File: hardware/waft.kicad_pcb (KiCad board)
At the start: 2 copper layers, 45 parts, among them IC1 VL6180x_Composite, J1 CONN_01X01, J2 Thonkiconn, J3 Thonkiconn, J4 Thonkiconn, J5 Thonkiconn, J6 Thonkiconn, J7 Thonkiconn, U1 MCP4728, U2 TL071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

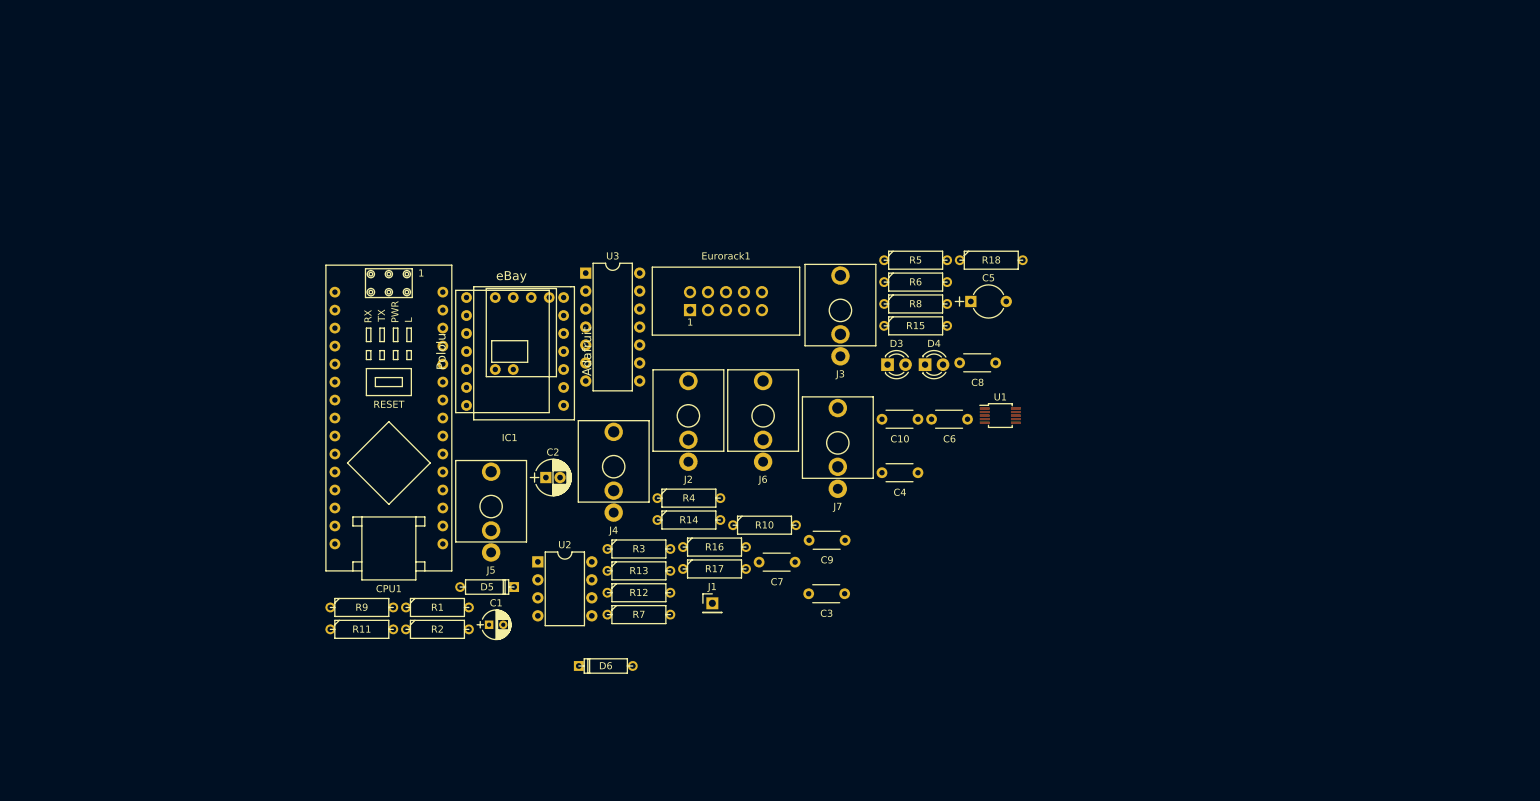
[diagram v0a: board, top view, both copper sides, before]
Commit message: Schematic changes.
Couple of changes to the schematic, & started laying out the PCB.
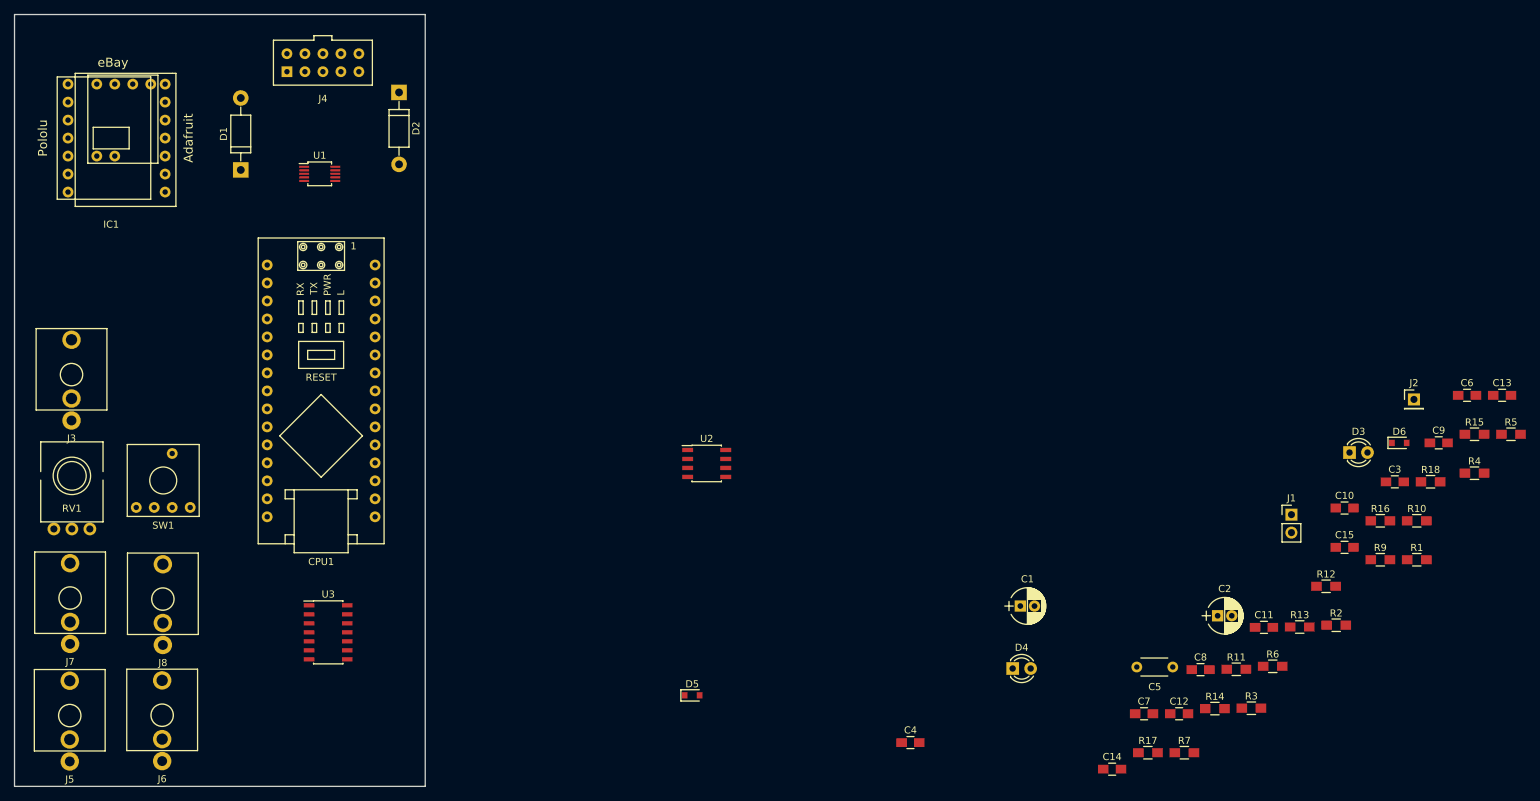
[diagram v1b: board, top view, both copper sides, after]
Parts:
- removed Eurorack1: CONN_02X05, Connect:IDC_Header_Straight_10pins
- removed R8: 100k, Discret:R3-5
- added C11: 47pF, Capacitors_SMD:C_0805_HandSoldering, F.Cu at (217.3, 137.9)
- added C12: 47pF, Capacitors_SMD:C_0805_HandSoldering, F.Cu at (205.3, 150.1)
- added C13: 47pF, Capacitors_SMD:C_0805_HandSoldering, F.Cu at (250.9, 105.2)
- added C14: 47pF, Capacitors_SMD:C_0805_HandSoldering, F.Cu at (195.9, 158.0)
- added C15: 47pF, Capacitors_SMD:C_0805_HandSoldering, F.Cu at (228.7, 126.6)
- added D1: 1N5817, Diodes_ThroughHole:D_DO-41_SOD81_P10.16mm_Horizontal, F.Cu at (72.8, 73.3)
- added D2: 1N5817, Diodes_ThroughHole:D_DO-41_SOD81_P10.16mm_Horizontal, F.Cu at (95.2, 62.4)
- added J8: Thonkiconn, europi:Thonkiconn, F.Cu at (61.8, 133.9)
- added RV1: B100K, europi:Alpha_9mm_Vertical, F.Cu at (49.0, 116.5)
- added SW1: Coded_Switch, europi:10_Way_Coded_Switch, F.Cu at (61.9, 117.2)
- C1: footprint Capacitors_ThroughHole:CP_Radial_D4.0mm_P2.00mm -> Capacitors_ThroughHole:CP_Radial_D5.0mm_P2.00mm
- C10, C3, C4, C6, C7, C8, C9: footprint europi:tantalum_capacitor -> Capacitors_SMD:C_0805_HandSoldering
- C5: footprint Capacitors_ThroughHole:CP_Radial_Tantal_D4.5mm_P5.00mm -> europi:tantalum_capacitor
- D5, D6: footprint Discret:D3 -> Diodes_SMD:D_0805
- J1: value CONN_01X01 -> CONN_01X02; footprint Pin_Headers:Pin_Header_Straight_1x01_Pitch2.54mm -> Pin_Headers:Pin_Header_Straight_1x02_Pitch2.54mm
- J2: value Thonkiconn -> CONN_01X01; footprint europi:Thonkiconn -> Pin_Headers:Pin_Header_Straight_1x01_Pitch2.54mm
- J4: value Thonkiconn -> Conn_02x05_Odd_Even; footprint europi:Thonkiconn -> europi:IDC-2x5
- R1, R10, R11, R12, R13, R14, R15, R16, R17, R18, R2, R3, R4, R5, R6, R7, R9: footprint Discret:R3-5 -> Resistors_SMD:R_0805_HandSoldering
- U2: footprint Housings_DIP:DIP-8_W7.62mm -> Housings_SOIC:SOIC-8_3.9x4.9mm_Pitch1.27mm
- U3: footprint Housings_DIP:DIP-14_W7.62mm -> Housings_SOIC:SOIC-14_3.9x8.7mm_Pitch1.27mm
- moved R9 144.0 mm to (233.7, 128.4)
- moved R1 138.5 mm to (238.9, 128.4)
- moved R2 126.9 mm to (227.5, 137.6)
- moved R11 123.6 mm to (213.4, 143.9)
- moved D6 116.4 mm to (236.4, 111.9), turned to 0 degrees
- moved R4 111.0 mm to (247.0, 116.2)
- moved J7 110.6 mm to (48.7, 133.8)
- moved J3 109.0 mm to (48.9, 102.2)
- moved J2 102.5 mm to (238.5, 105.8)
- moved U1 102.0 mm to (84.0, 73.9)
- moved R12 97.0 mm to (226.1, 132.1)
- moved C2 96.8 mm to (210.8, 136.3)
- moved J6 94.8 mm to (61.7, 150.3)
- moved R16 94.1 mm to (233.7, 122.9)
- moved R13 93.7 mm to (222.3, 137.9)
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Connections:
- CPU1 pad 10: (no net) -> Net-(CPU1-Pad10)
- CPU1 pad 11: (no net) -> Net-(CPU1-Pad11)
- CPU1 pad 12: (no net) -> Net-(CPU1-Pad12)
- CPU1 pad 13: (no net) -> Net-(CPU1-Pad13)
- CPU1 pad 9: (no net) -> DIR
- J1 pad 1: Net-(J1-Pad1) -> GND
- J2 pad 1: GND -> Net-(J2-Pad1)
- J3 pad 2: (no net) -> GND
- J4 pad 1: GND -> Net-(D1-Pad2)
- J4 pad 2: (no net) -> Net-(D1-Pad2)
- J4 pad 3: Net-(D5-Pad1) -> GND
- J5 pad 3: Net-(D6-Pad1) -> Net-(D5-Pad1)
- J6 pad 3: Net-(J6-Pad3) -> Net-(D6-Pad1)
- R1 pad 1: Net-(J1-Pad1) -> Net-(J2-Pad1)
- R17 pad 1: Net-(J6-Pad3) -> Net-(J7-Pad3)
- R18 pad 1: Net-(J7-Pad3) -> Net-(J8-Pad3)
- R2 pad 2: Net-(J1-Pad1) -> Net-(J2-Pad1)
- R4 pad 1: Net-(R4-Pad1) -> Net-(C15-Pad1)
- R5 pad 2: Net-(J2-Pad3) -> Net-(J3-Pad3)
- R6 pad 2: Net-(R4-Pad1) -> Net-(R6-Pad2)
- U2 pad 6: Net-(R4-Pad1) -> Net-(C15-Pad1)
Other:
- board outline added: 58 x 109 mm
- rule pad_to_mask_clearance: 0.2 -> 0

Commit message: Started board layout
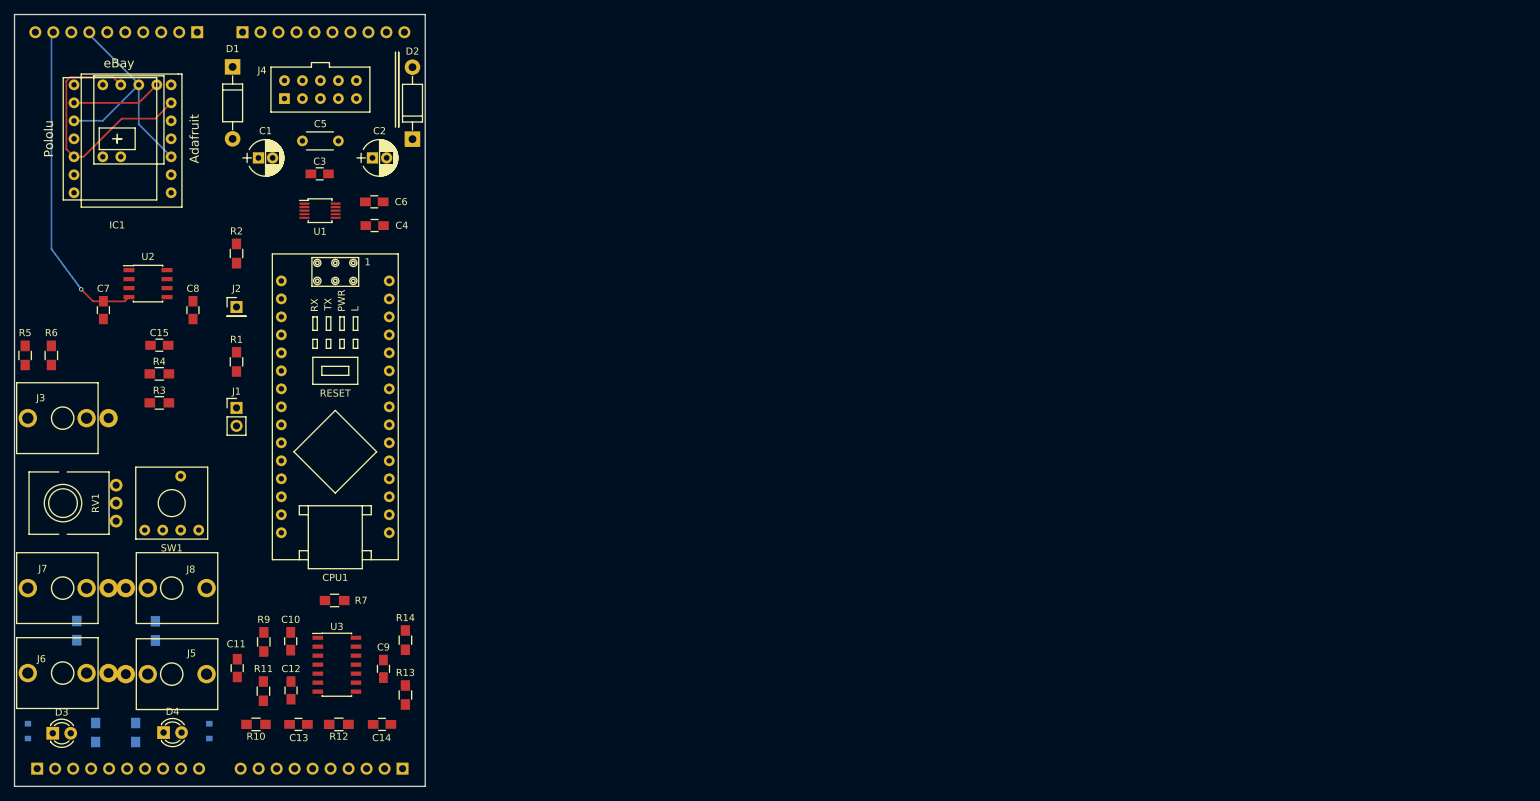
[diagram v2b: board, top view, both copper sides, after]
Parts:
- added J10: Conn_01x10_Female, Pin_Headers:Pin_Header_Straight_1x10_Pitch2.54mm, B.Cu at (95.7, 157.9)
- added J11: Conn_01x10_Male, Pin_Headers:Pin_Header_Straight_1x10_Pitch2.54mm, B.Cu at (66.7, 53.9)
- added J12: Conn_01x10_Male, Pin_Headers:Pin_Header_Straight_1x10_Pitch2.54mm, B.Cu at (44.0, 157.9)
- added J9: Conn_01x10_Female, Pin_Headers:Pin_Header_Straight_1x10_Pitch2.54mm, B.Cu at (73.0, 53.9)
- D5, D6, R15, R16, R17, R18: moved to B.Cu
- moved R5 210.1 mm to (42.4, 99.5), turned to 270 degrees
- moved R15 199.2 mm to (52.3, 152.8), turned to 270 degrees
- moved D3 187.4 mm to (46.2, 152.9)
- moved R4 186.3 mm to (61.3, 102.2), turned to 180 degrees
- moved R18 181.3 mm to (60.8, 138.4), turned to 270 degrees
- moved R16 178.3 mm to (58.0, 152.8), turned to 270 degrees
- moved R6 178.0 mm to (46.0, 99.5), turned to 270 degrees
- moved C13 176.2 mm to (81.0, 151.7), turned to 180 degrees
- moved D6 172.9 mm to (68.3, 152.6), turned to 270 degrees
- moved C15 169.8 mm to (61.3, 98.1), turned to 180 degrees
- moved R1 169.0 mm to (72.2, 100.5), turned to 270 degrees
- moved J2 166.8 mm to (72.2, 92.7)
- moved R10 166.4 mm to (75.0, 151.7), turned to 180 degrees
- moved R2 163.9 mm to (72.2, 85.2), turned to 270 degrees
- moved R3 160.1 mm to (61.3, 106.2)
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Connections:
- C11 pad 2: Net-(C11-Pad2) -> MIXa
- C13 pad 1: Net-(C13-Pad1) -> CV1a
- C14 pad 1: Net-(C14-Pad1) -> CV2a
- C6 pad 1: DAC_B -> DAC_Ba
- CPU1 pad 10: Net-(CPU1-Pad10) -> DOa
- CPU1 pad 11: Net-(CPU1-Pad11) -> D1a
- CPU1 pad 12: Net-(CPU1-Pad12) -> D2a
- CPU1 pad 13: Net-(CPU1-Pad13) -> D3a
- CPU1 pad 23: SDA -> SDAa
- CPU1 pad 24: SCL -> SCLa
- CPU1 pad 5: GATE_1 -> GATE_1a
- CPU1 pad 6: GATE_2 -> GATE_2a
- D5 pad 2: GATE_1 -> GATE_1b
- D6 pad 2: GATE_2 -> GATE_2b
- IC1 pad 19: SCL -> SCLb
- IC1 pad 20: SDA -> SDAb
- IC1 pad 4: SDA -> SDAb
- IC1 pad 5: SCL -> SCLb
- IC1 pad 8: SDA -> SDAb
- IC1 pad 9: SCL -> SCLb
- R13 pad 1: Net-(C13-Pad1) -> CV1a
- R14 pad 1: Net-(C14-Pad1) -> CV2a
- R15 pad 2: GATE_1 -> GATE_1b
- R16 pad 2: GATE_2 -> GATE_2b
- R17 pad 2: Net-(C13-Pad1) -> CV1b
- R18 pad 2: Net-(C14-Pad1) -> CV2b
- R5 pad 1: Net-(C11-Pad2) -> MIXb
- R6 pad 1: Net-(C11-Pad2) -> MIXb
- R9 pad 2: Net-(C11-Pad2) -> MIXa
- SW1 pad 2: Net-(CPU1-Pad10) -> D0b
- SW1 pad 3: Net-(CPU1-Pad11) -> D1b
- SW1 pad 4: Net-(CPU1-Pad12) -> D2b
- SW1 pad 5: Net-(CPU1-Pad13) -> D3b
- U1 pad 2: SCL -> SCLa
- U1 pad 3: SDA -> SDAa
- U1 pad 7: DAC_B -> DAC_Ba
- U2 pad 3: DAC_B -> DAC_Bb
- U3 pad 14: Net-(C14-Pad1) -> CV2a
- U3 pad 2: Net-(C11-Pad2) -> MIXa
- U3 pad 8: Net-(C13-Pad1) -> CV1a
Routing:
- net SCLb: track 0.00 -> 74.0 mm
- net GND: track 0.00 -> 23.4 mm
- net +3V3: track 0.00 -> 12.7 mm
- net MIXb: track 0.00 -> 10.3 mm
- net -12V: track 0.00 -> 7.67 mm, vias 0 -> 1

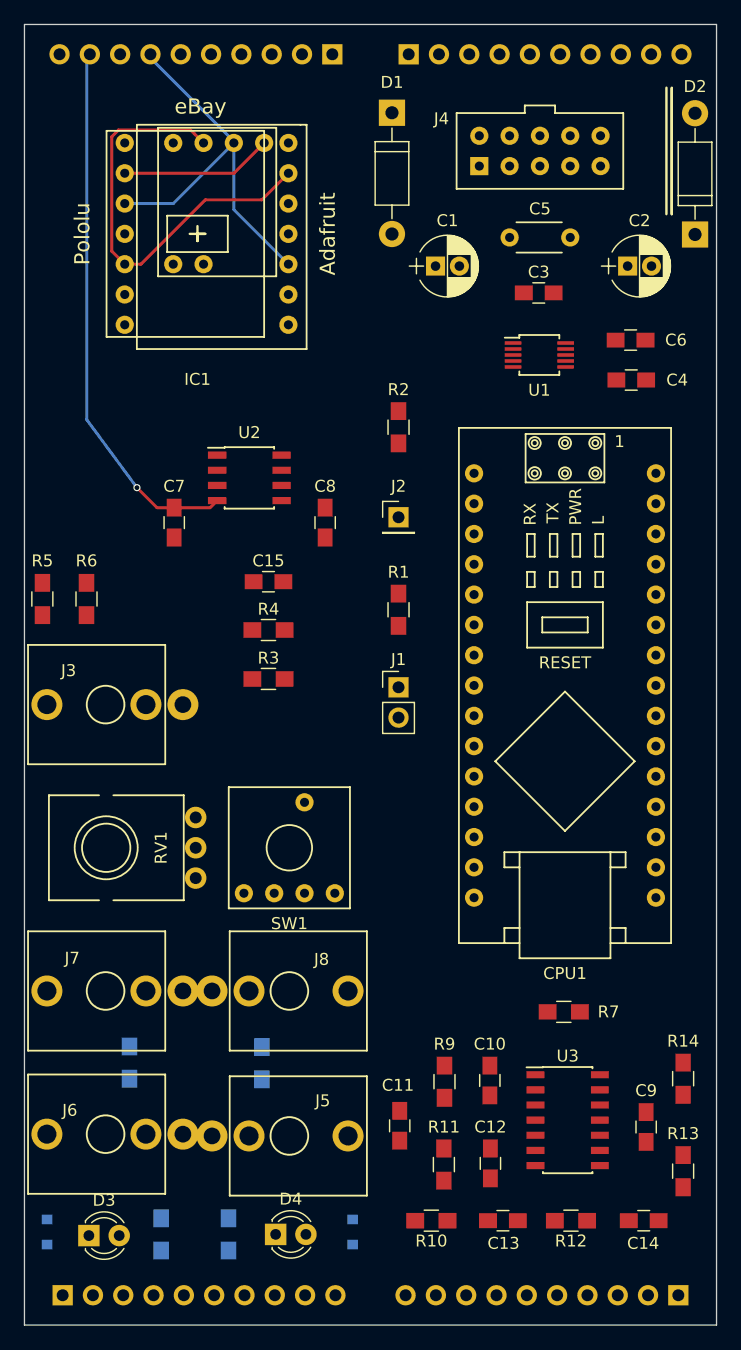
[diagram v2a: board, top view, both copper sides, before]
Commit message: Top and bottom track routing
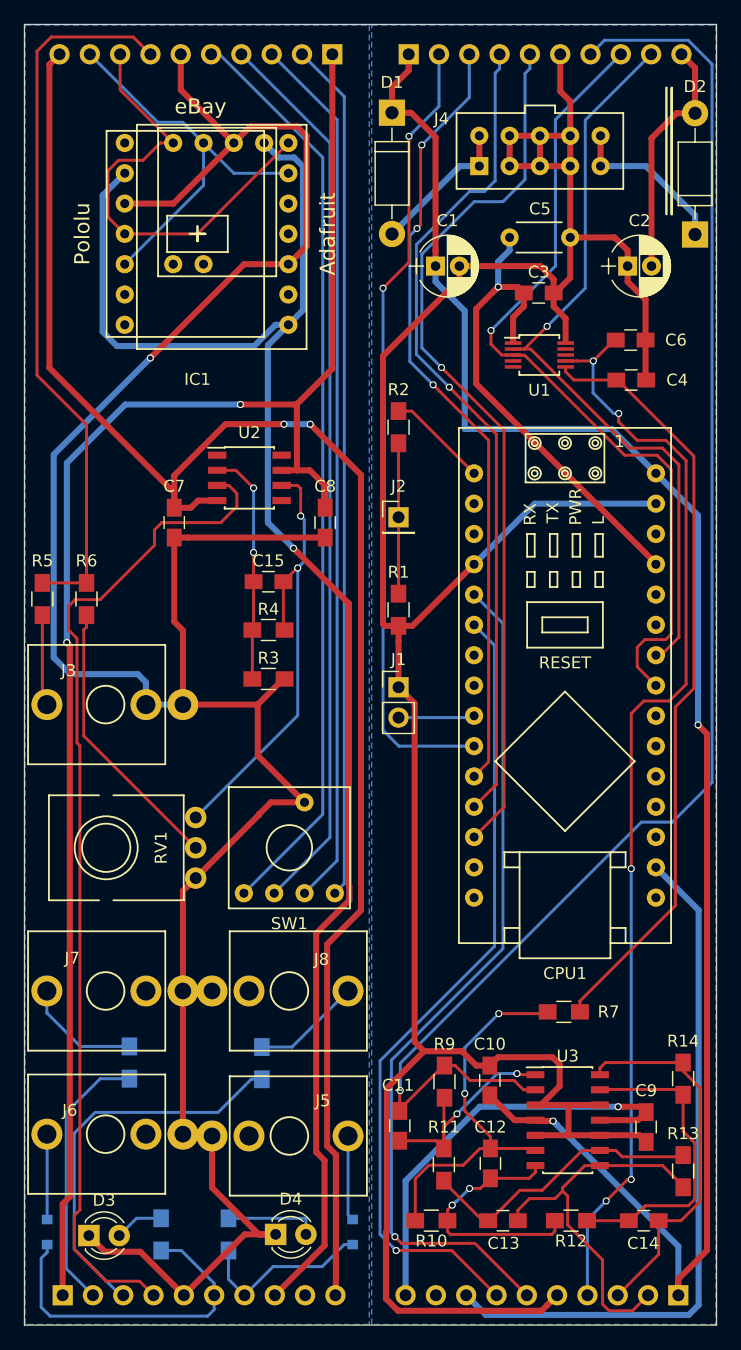
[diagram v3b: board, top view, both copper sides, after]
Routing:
- net GND: track 23.4 -> 446.9 mm, vias 0 -> 1
- net +12V: track 0.00 -> 283.4 mm, vias 0 -> 4
- net -12V: track 7.67 -> 195.2 mm, vias 1 -> 3
- net +3V3: track 12.7 -> 195.4 mm, vias 0 -> 1
- net MIXa: track 0.00 -> 125.5 mm, vias 0 -> 1
- net DAC_Ba: track 0.00 -> 93.0 mm, vias 0 -> 5
- net DAC_Bb: track 0.00 -> 84.1 mm
- net D3b: track 0.00 -> 77.3 mm
- net D2b: track 0.00 -> 75.3 mm
- net D3a: track 0.00 -> 74.7 mm, vias 0 -> 1
- net D1b: track 0.00 -> 73.7 mm
- net D0b: track 0.00 -> 72.1 mm
- net GATE_1a: track 0.00 -> 71.9 mm, vias 0 -> 1
- net D2a: track 0.00 -> 70.2 mm, vias 0 -> 1
- net SDAa: track 0.00 -> 69.2 mm, vias 0 -> 1
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- added copper zone on B.Cu, net GND
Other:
- net class Power added: clearance 0.2, trace_width 0.508, via_dia 0.6, via_drill 0.4
